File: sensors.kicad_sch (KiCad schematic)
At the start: 21 parts, among them J501 BMV080, U501 SCD40-D-R2, U502 AS3935-BQFT, U503 BME688, U504 BME688

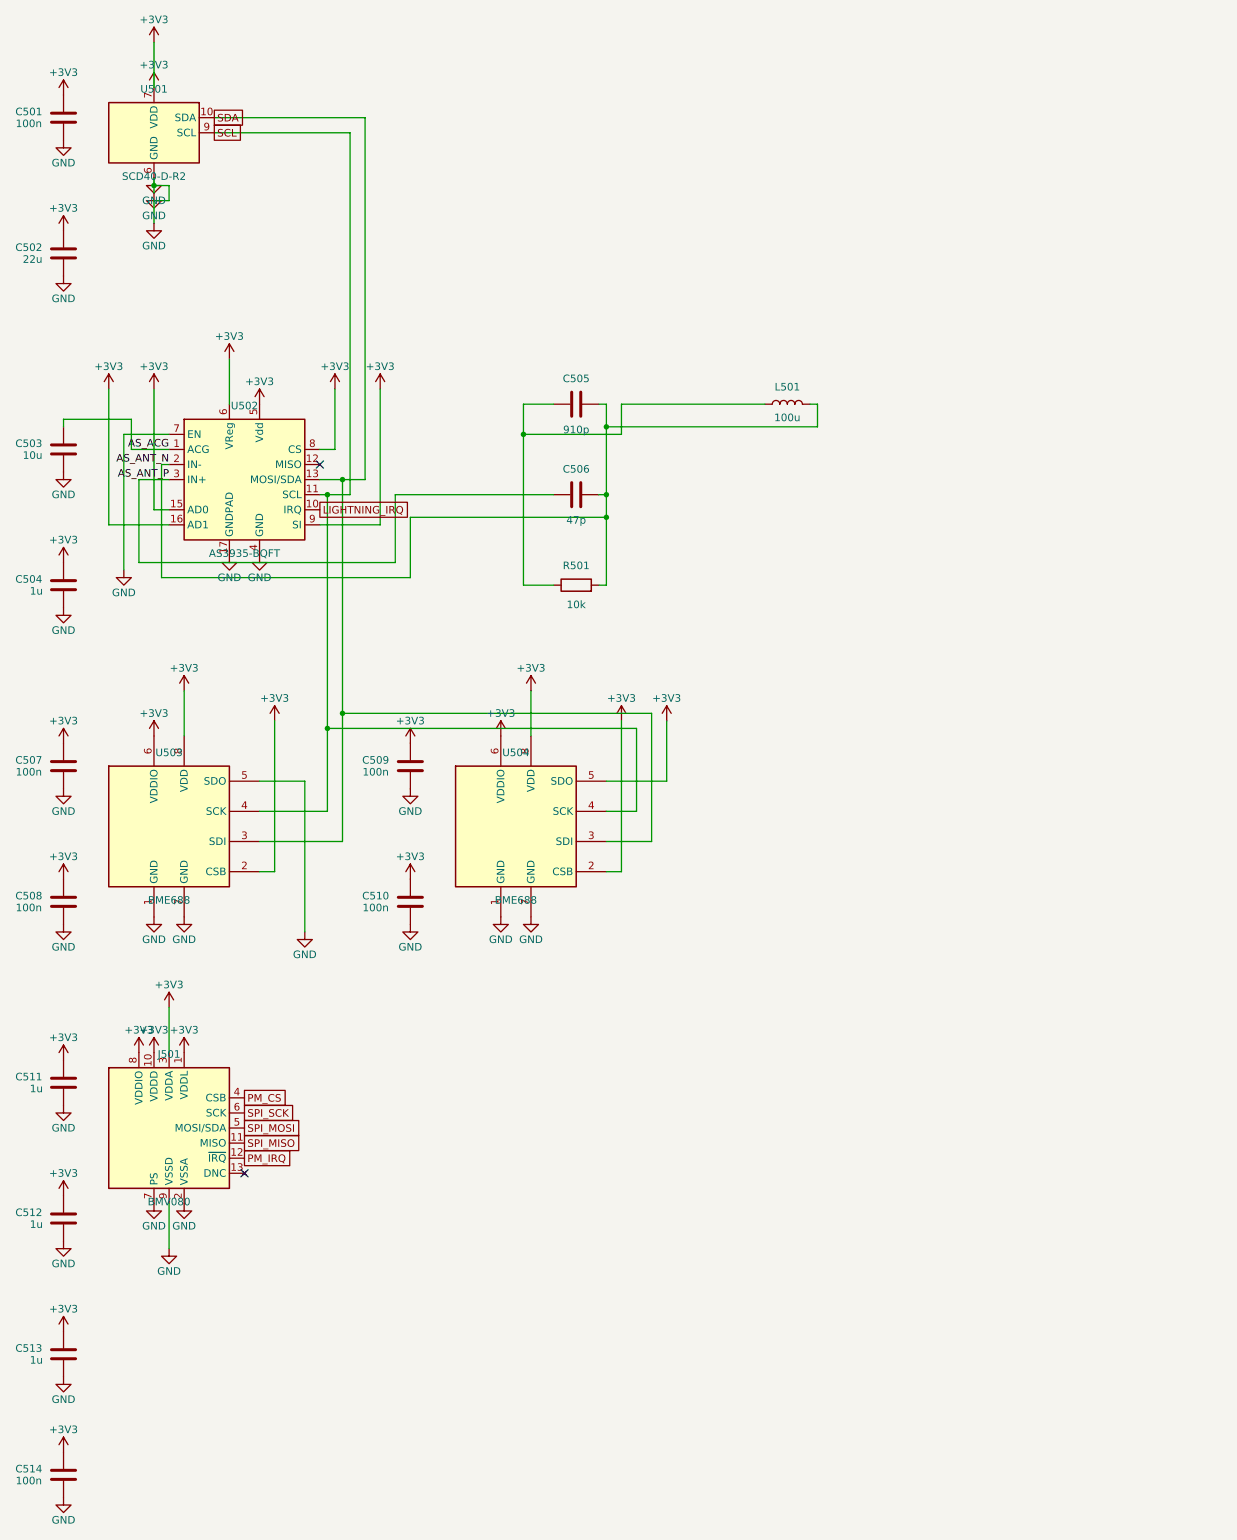
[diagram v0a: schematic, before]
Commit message: Remove the buck-boost: run straight off a 3.6 V max cell
The TPS63001 and its inductor come out and the battery drives the board
directly, so the rail is renamed +3V3 -> +BATT on every sheet: a net called
3V3 that is really the cell is the kind of label someone connects a charger
to.

SW101 used to switch the converter's EN pin, which is why it was never in
series with the load - the C&K JS series is rated 300 mA and this board
peaks past that. With no EN pin it now drives the gate of Q102, a second
DMG3401LSN-7 back to back with the reverse-block Q101. Q101 keeps its source
on the load side so its body diode conducts forward, which is exactly why it
cannot also be the switch; Q102 faces the other way so an open channel
really disconnects.

R102/C102 are re-used as a 10k/1u gate network giving about 9 ms of soft
start, replacing the converter's. Without it the switch would connect ~70 uF
of rail and IC decoupling straight across a cell that may have ohms of
internal resistance. The 10k stays small against the 100k pull-up so the
gate still reaches 91 % of VBATT.

The R103/R104 sense divider moves from VBATT to the switched +BATT, so it
draws nothing with the board off.

Also fixes assemble.ts rewriting cc1200_balloon.kicad_pro from a fixed
template every build, which was silently resetting the net classes, board
design settings and ERC severities KiCad had written. Found while rebuilding
for this change.

Gates: placement 5/5, routing DRC 0, netlist matches sheets/*.json at 378
endpoints / 76 nets, full-hierarchy ERC 0 errors and the 2 known BME688
address-strap warnings. Build output is byte-identical across runs.

The large .kicad_sch diffs are formatting: the committed set had been opened
and saved by KiCad, which expands the compact s-expressions the generator
writes. Nothing but the power sheet and the rail name changed electrically.

Not done: cc1200_balloon.kicad_pcb still carries U101, L101 and C105 and has
no Q102. It needs Update PCB from Schematic.

Co-Au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
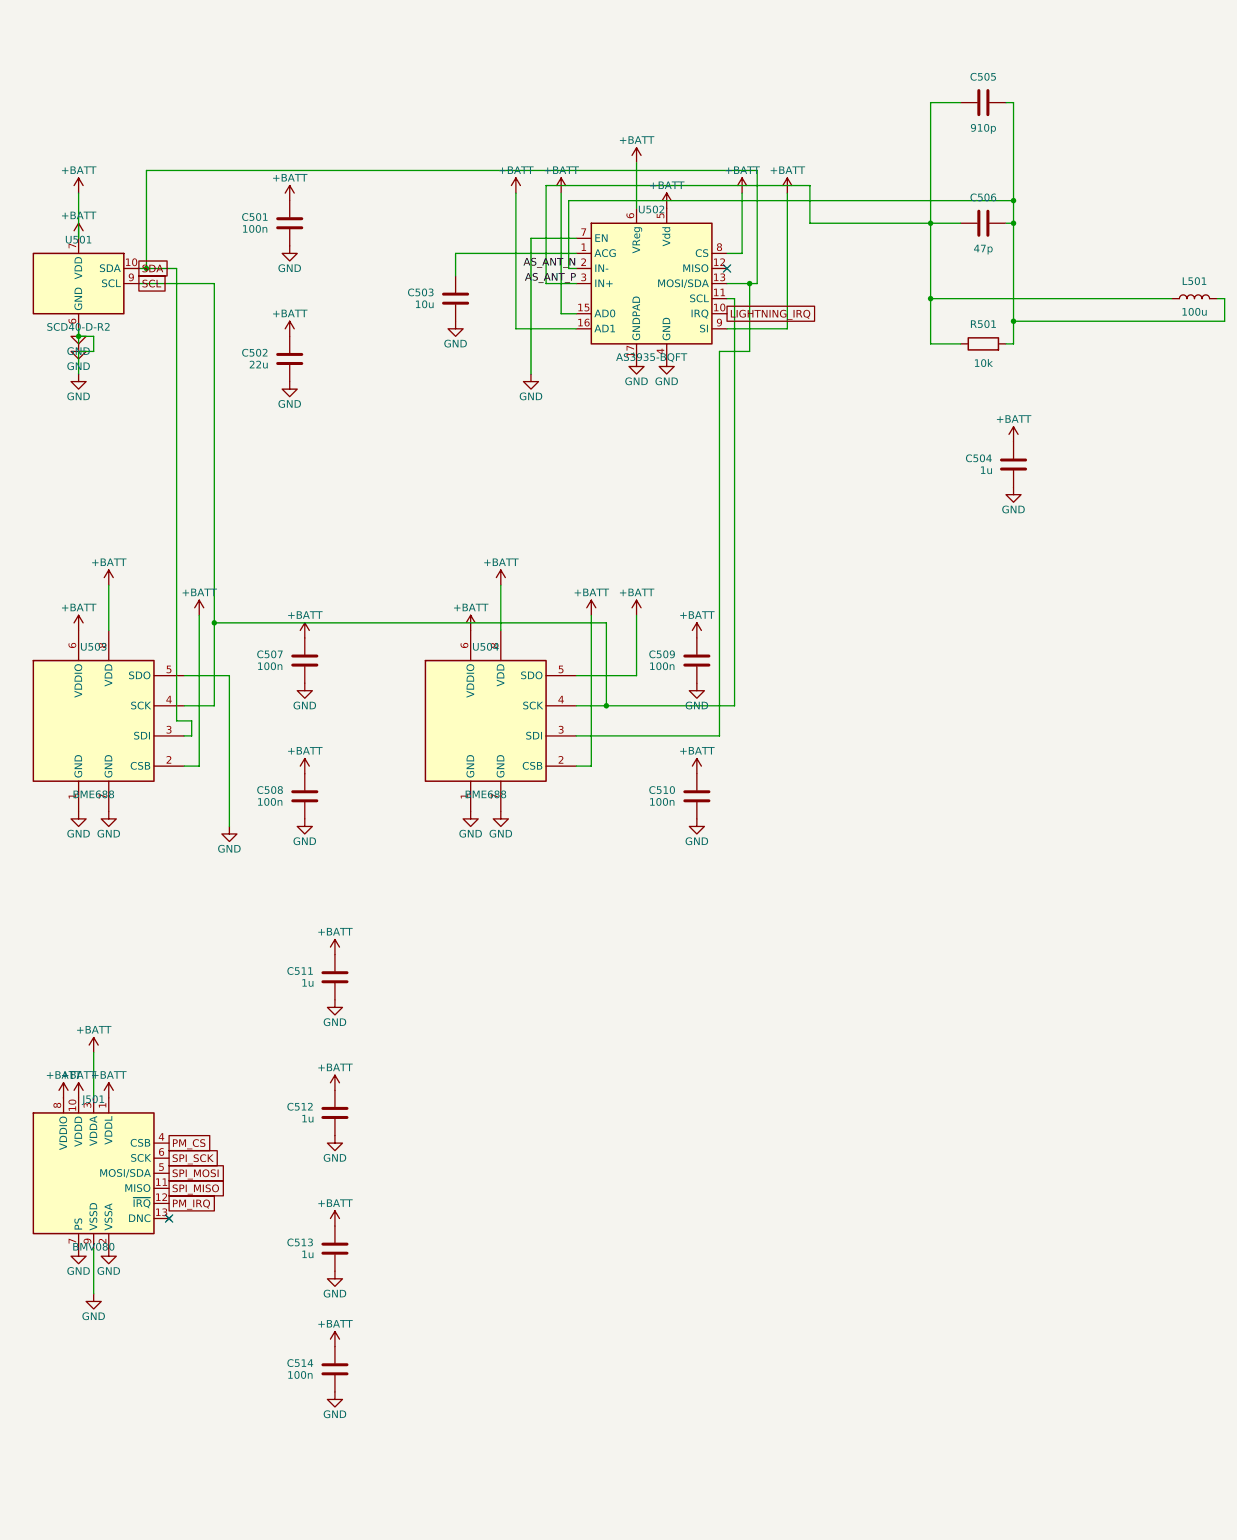
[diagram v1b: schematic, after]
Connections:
- net AS_ANT_P: now also C505.1, L501.1, R501.1
- net +3V3 renamed +BATT
- net AS_ACG: no longer names the net of C503.1, U502.1 (ACG)
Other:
- moved on the sheet: C501, C502, C503, C504, C505, C506, C507, C508, C509, C510, C511, C512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
